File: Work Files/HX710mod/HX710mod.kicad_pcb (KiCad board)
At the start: 2 copper layers, 64.8 x 59.7 mm, 10 parts

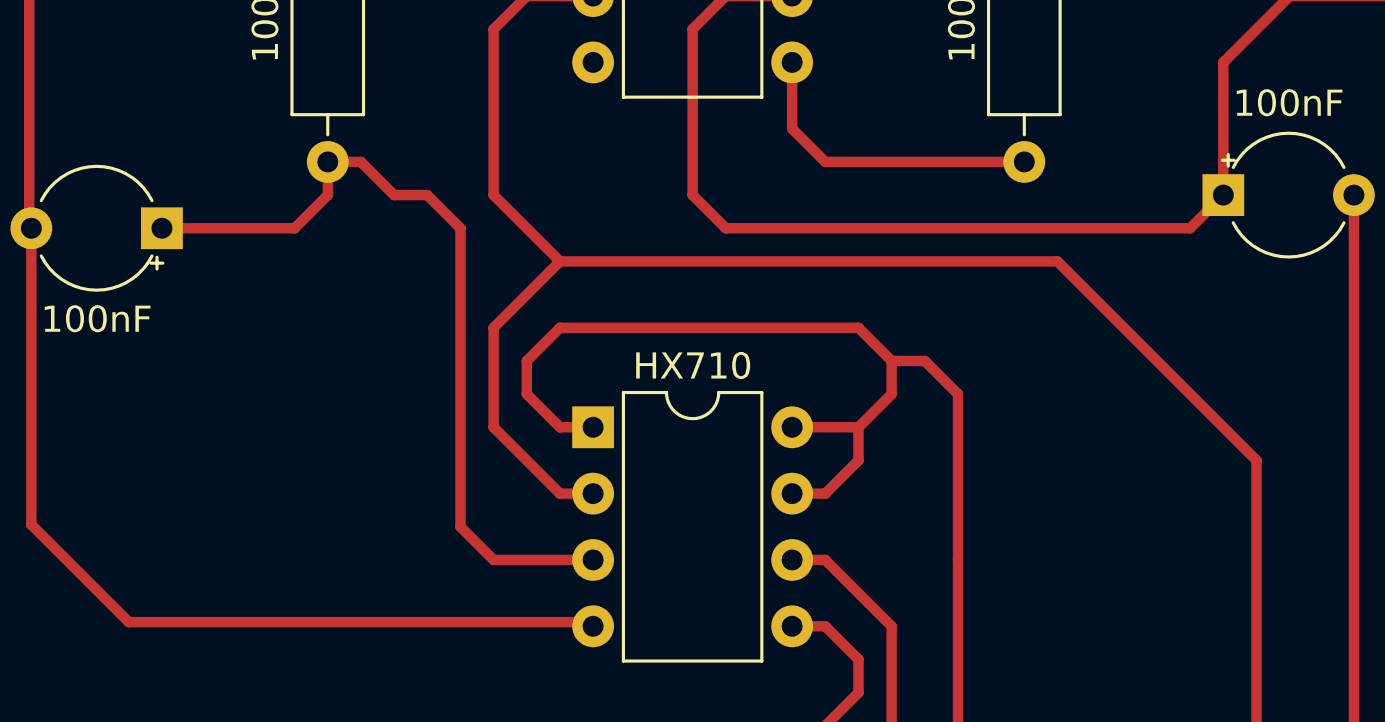
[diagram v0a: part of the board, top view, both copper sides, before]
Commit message: Added temporary design for HX710B module2
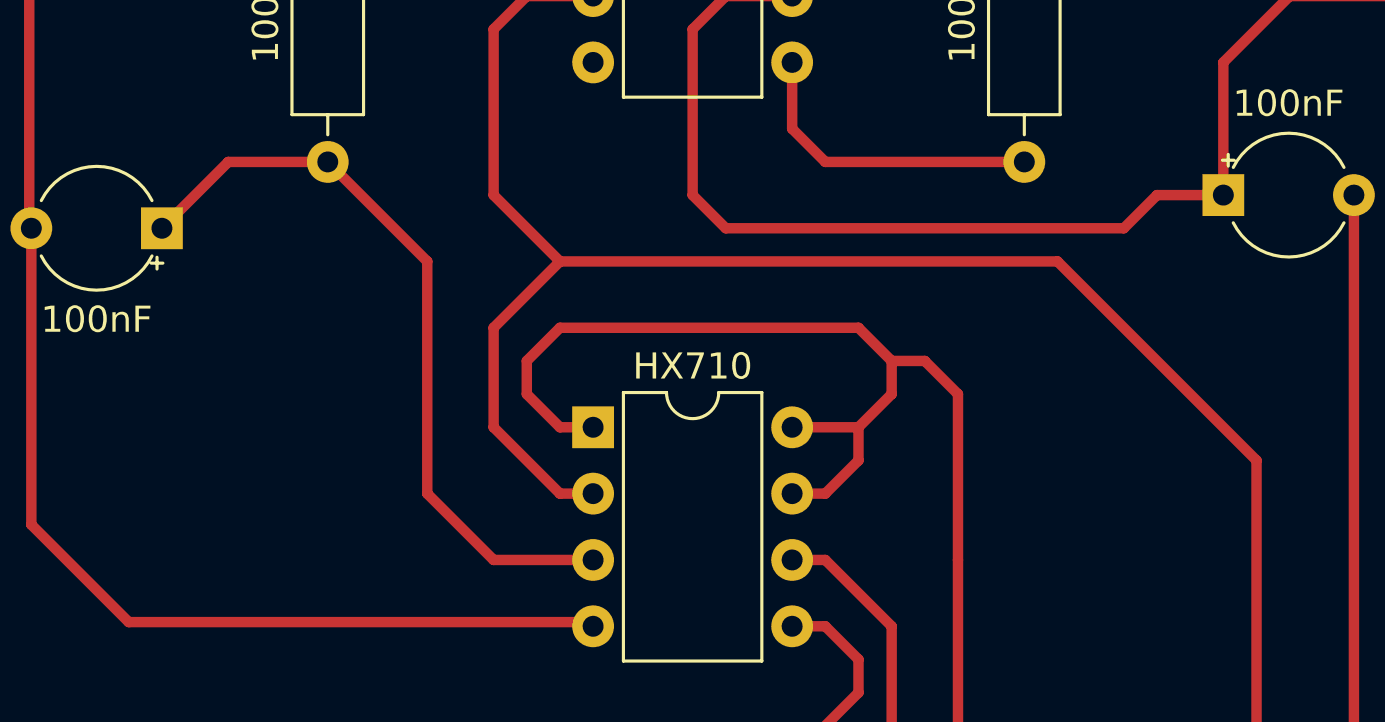
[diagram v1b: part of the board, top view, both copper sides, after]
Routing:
- net (no net): track 500.3 -> 498.1 mm
